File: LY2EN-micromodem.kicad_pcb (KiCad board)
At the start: 2 copper layers, 20.4 x 63.5 mm, 20 parts, among them Q1 2N7000

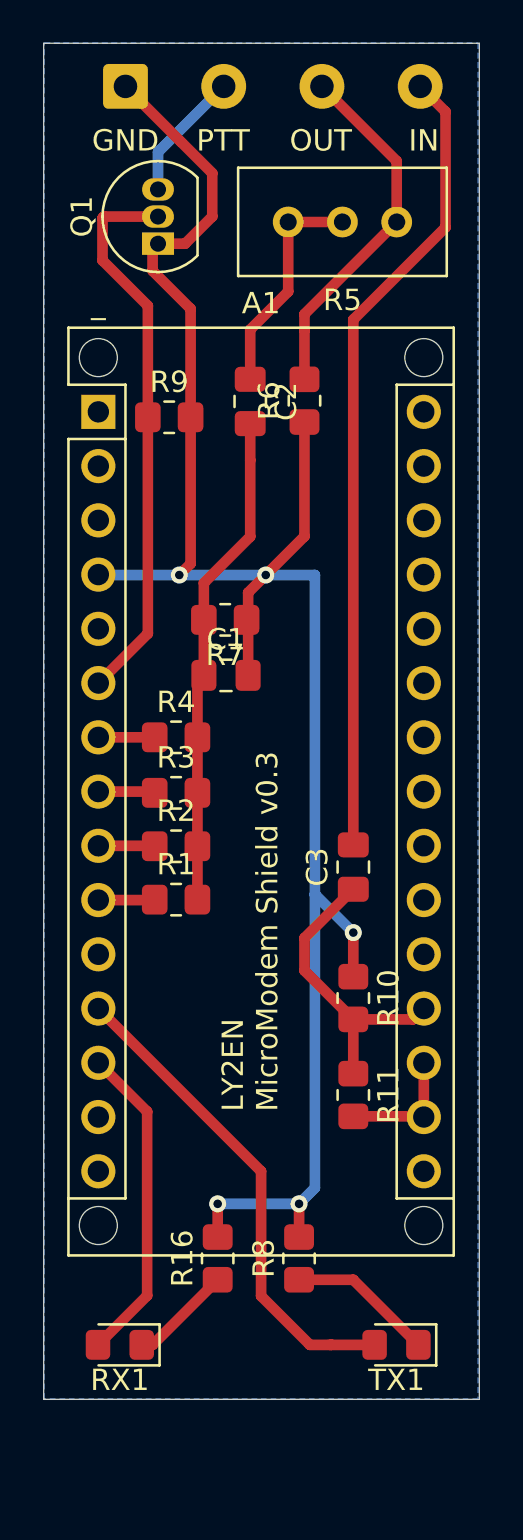
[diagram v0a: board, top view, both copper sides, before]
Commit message: Add Bluetooth SPP-C serial passthrough support
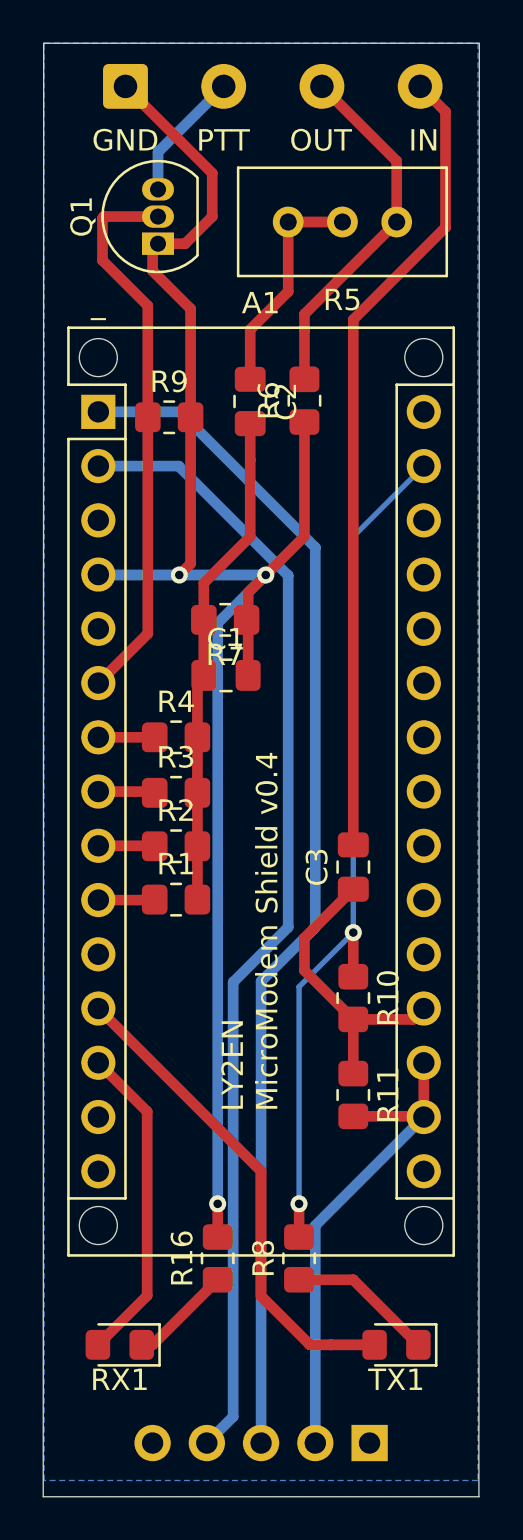
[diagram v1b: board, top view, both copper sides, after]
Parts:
- added Conn_01x05: BT_MOD, Connector_PinSocket_2.54mm:PinSocket_1x05_P2.54mm_Vertical, B.Cu at (99.1, 96.5)
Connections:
- A1 pad 11: Net-(A1-Pad11) -> unconnected-(A1-Pad11)
- A1 pad 14: Net-(A1-Pad14) -> unconnected-(A1-Pad14)
- A1 pad 15: Net-(A1-Pad15) -> unconnected-(A1-Pad15)
- A1 pad 16: Net-(A1-Pad16) -> unconnected-(A1-Pad16)
- A1 pad 20: Net-(A1-Pad20) -> unconnected-(A1-Pad20)
- A1 pad 21: Net-(A1-Pad21) -> unconnected-(A1-Pad21)
- A1 pad 22: Net-(A1-Pad22) -> unconnected-(A1-Pad22)
- A1 pad 23: Net-(A1-Pad23) -> unconnected-(A1-Pad23)
- A1 pad 24: Net-(A1-Pad24) -> unconnected-(A1-Pad24)
- A1 pad 25: Net-(A1-Pad25) -> unconnected-(A1-Pad25)
- A1 pad 26: Net-(A1-Pad26) -> unconnected-(A1-Pad26)
- A1 pad 27: Net-(A1-Pad27) -> unconnected-(A1-Pad27)
- A1 pad 28: Net-(A1-Pad28) -> unconnected-(A1-Pad28)
- A1 pad 3: Net-(A1-Pad3) -> unconnected-(A1-Pad3)
- A1 pad 30: Net-(A1-Pad30) -> unconnected-(A1-Pad30)
- A1 pad 5: Net-(A1-Pad5) -> unconnected-(A1-Pad5)
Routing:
- net Net-(Conn_01x05-Pad3): track 0.00 -> 55.8 mm
- net Net-(Conn_01x05-Pad4): track 0.00 -> 53.2 mm
- net GND: track 91.8 -> 120.7 mm
- net Net-(A1-Pad17): track 5.86 -> 23.2 mm
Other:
- board size 20.4 x 63.5 mm -> 20.4 x 68.1 mm
- board text added: "LY2EN MicroModem Shield v0.4"
- board text removed: "LY2EN MicroModem Shield v0.3"

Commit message: Replace potentiometer with static 47k resistor
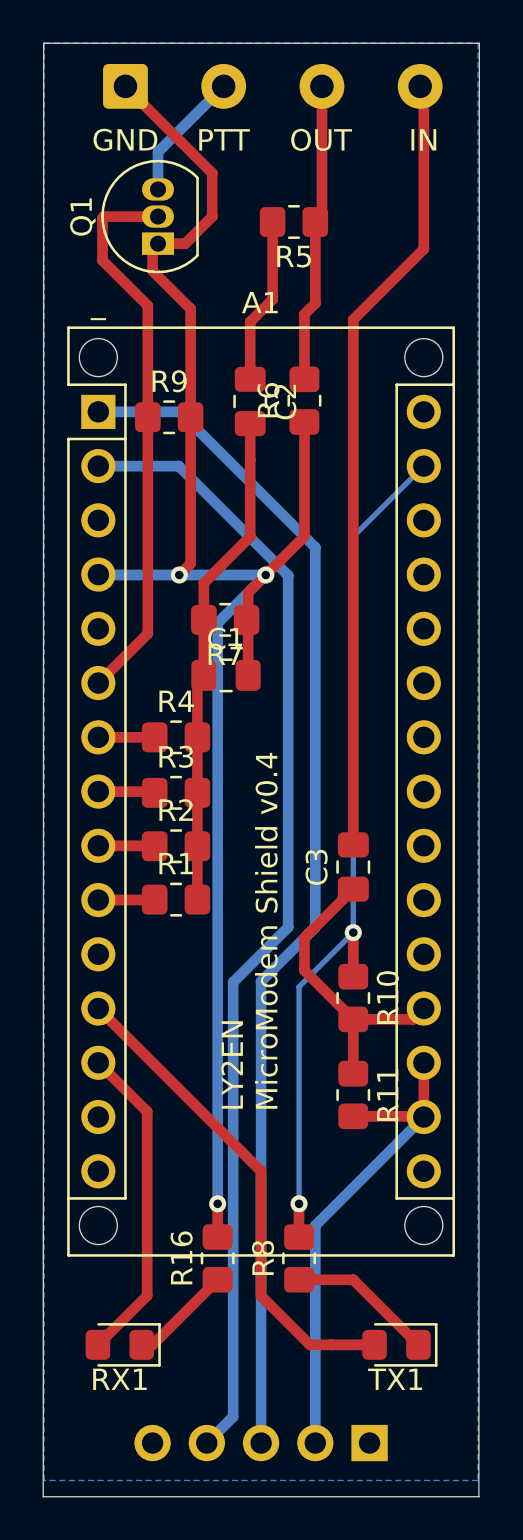
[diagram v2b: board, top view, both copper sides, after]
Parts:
- R5: value 100k -> 47k; footprint Potentiometer_THT:Potentiometer_Bourns_3296W_Vertical -> Resistor_SMD:R_0805_2012Metric_Pad1.20x1.40mm_HandSolder
- moved R5 0.27 mm to (95.5, 39.4)
- renumbered Conn_01x05 to Conn_01x5
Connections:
- R5 pad 1: Net-(C2-Pad1) -> ANALOG_OUT
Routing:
- net ANALOG_OUT: track 17.0 -> 14.1 mm
- net Net-(C2-Pad1): track 10.6 -> 7.80 mm
- net ANALOG_IN: track 37.8 -> 37.0 mm
